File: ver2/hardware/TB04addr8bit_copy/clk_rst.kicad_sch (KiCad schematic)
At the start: 30 parts, among them SW501 SW_Push, SW502 SW_Rotary_1x9_MP, SW503 SW_Push, U501 74HC14, U502 4060, Y501 32.768KHz

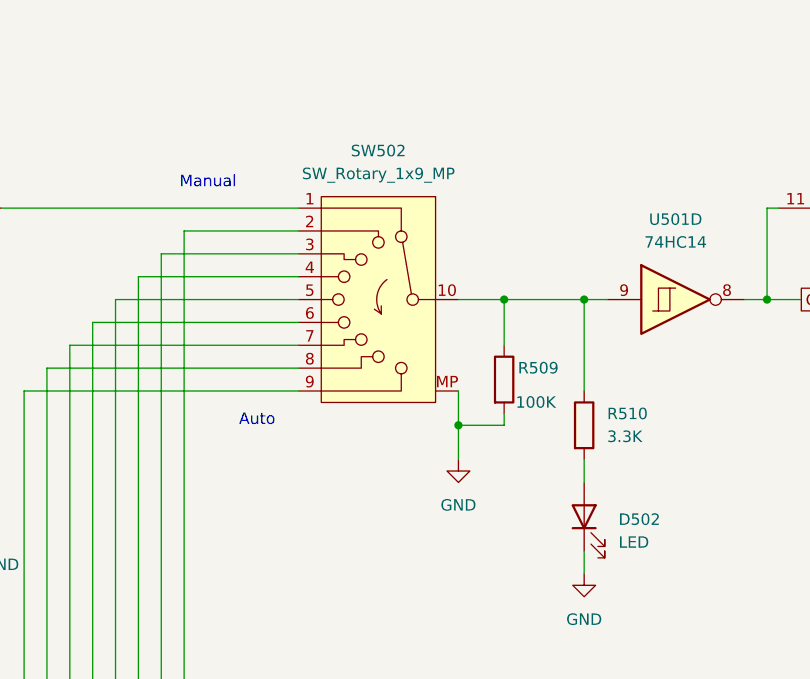
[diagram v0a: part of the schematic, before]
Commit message: ver2: ロータリースイッチSR1712F-0109のフットプリントを作成／SW502をrotarySW_01x09へ差し替え
- データシート(SLH-232)の埋め込み画像を読み、穴位置を実測して寸法を確定
  端子10-Ø0.9(2列×5・ピッチ2.5・列間18.3)、取付2-Ø2.0(間隔16.0・中点から1.1)
- KiCAD標準のSW_Rotary_1x9_MPは実物とピン番号が逆(pin10がコモン)だったため
  My_Lib:rotarySW_01x09(pin1=コモン)へ差し替え。実物・シンボル・FPが三者一致
- pcbnewのAPIでパッド12個の座標を全数検証
- マスターにfp-lib-tableを追加(footprints/Library.pretty)

Co-Authored-By: Claude Opus 5 <noreply@anthropic.com>
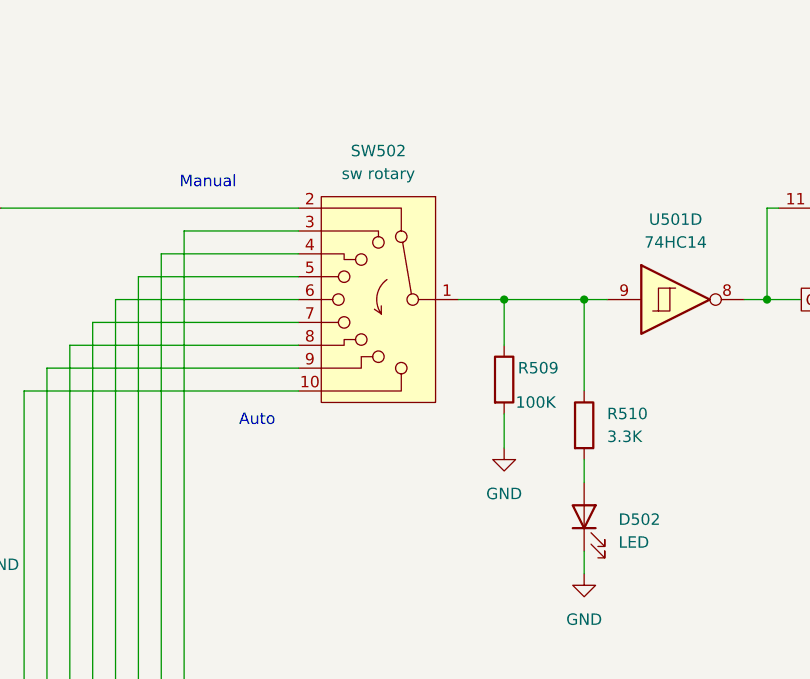
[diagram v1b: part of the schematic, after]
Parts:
- removed SW502: SW_Rotary_1x9_MP, symbol Switch:SW_Rotary_1x9_MP
- added SW502: sw rotary, LibraryTB04:SW_Rotary_1x9_Alpha_SR1712F-0109, symbol My_Lib:rotarySW_01x09
- C505, C506: footprint (none) -> Capacitor_THT:C_Disc_D4.3mm_W1.9mm_P5.00mm
- R509: footprint (none) -> Resistor_THT:R_Axial_DIN0207_L6.3mm_D2.5mm_P7.62mm_Horizontal
- R511, R512: footprint (none) -> Resistor_THT:R_Axial_DIN0207_L6.3mm_D2.5mm_P10.16mm_Horizontal
- U502: footprint (none) -> Package_DIP:DIP-16_W7.62mm_Socket
- Y501: footprint (none) -> Package_DIP:DIP-8_W7.62mm_Socket
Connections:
- net at R509.1, R510.1, U501.9: now also SW502.1
- net at U502.1 (Q12): now also SW502.4
- net at U502.13 (Q9): now also SW502.6
- net at U502.14 (Q8): now also SW502.7
- net at U502.15 (Q10): now also SW502.5
- net at U502.2 (Q13): now also SW502.3
- net at U502.4 (Q6): now also SW502.8
- net at U502.5 (Q5): now also SW502.9
- net at U502.7 (Q4): now also SW502.10
- net at R505.2: now also SW502.2

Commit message: ver2: PCBの粗配置を自動生成(回路図シートごとのブロック配置)
- 参照番号の百の位でグループ化し、各グループを矩形にまとめて配置
- グループ間の接続本数から順序を焼きなましで最適化(蛇行配置)
- 部品の重なり0・グループ矩形の重なり0を確認
- 基板内202個/はみ出し77個(3段目の下半分)。配線は未着手

Co-Authored-By: Claude Opus 5 <noreply@anthropic.com>
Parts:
- Y501: footprint Package_DIP:DIP-8_W7.62mm_Socket -> Connector_PinSocket_2.00mm:PinSocket_1x02_P2.00mm_Vertical
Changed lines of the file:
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@@
 			)
 		)
-		(property "Footprint" "Package_DIP:DIP-8_W7.62mm_Socket"
+		(property "Footprint" "Connector_PinSocket_2.00mm:PinSocket_1x02_P2.00mm_Vertical"
 			(at 217.17 189.23 0)
 			(hide yes)
